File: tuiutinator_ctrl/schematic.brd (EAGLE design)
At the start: 87.3 x 63.5 mm, 13 parts

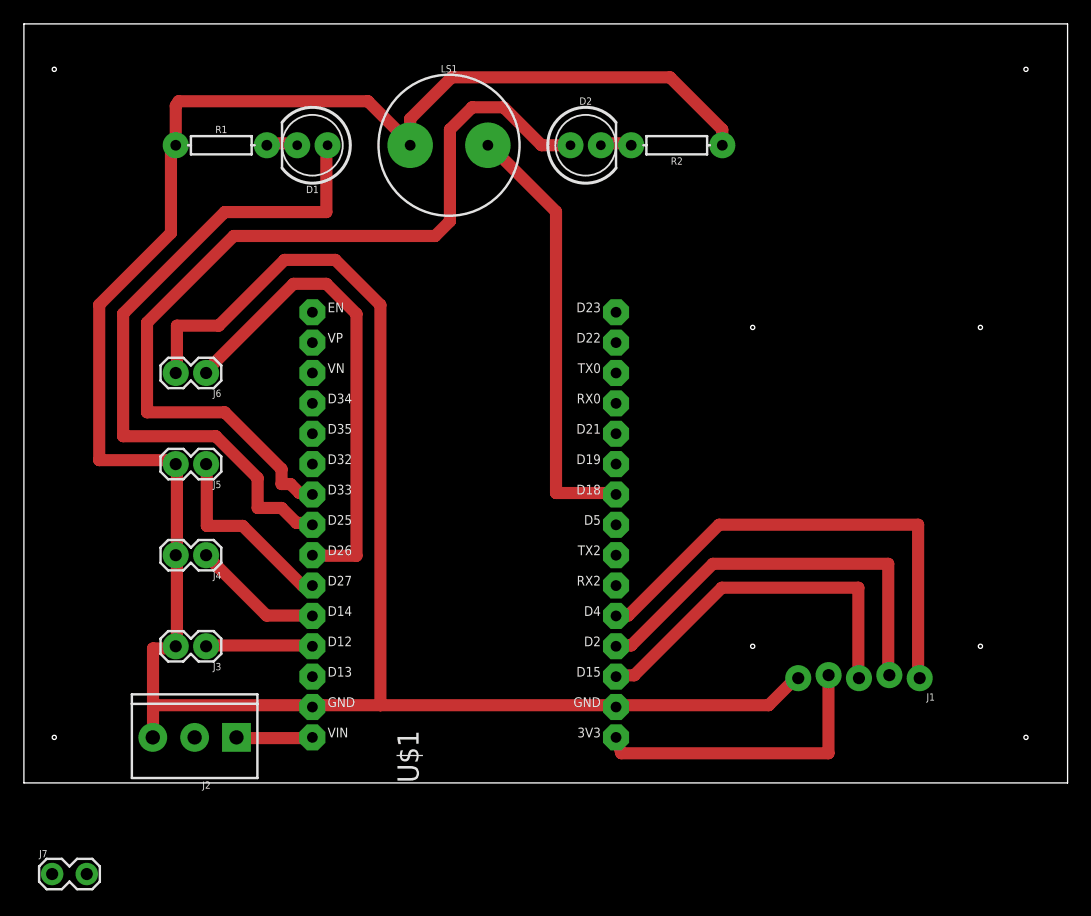
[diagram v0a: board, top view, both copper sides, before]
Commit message: Versão com controle pronto enviado para JLC
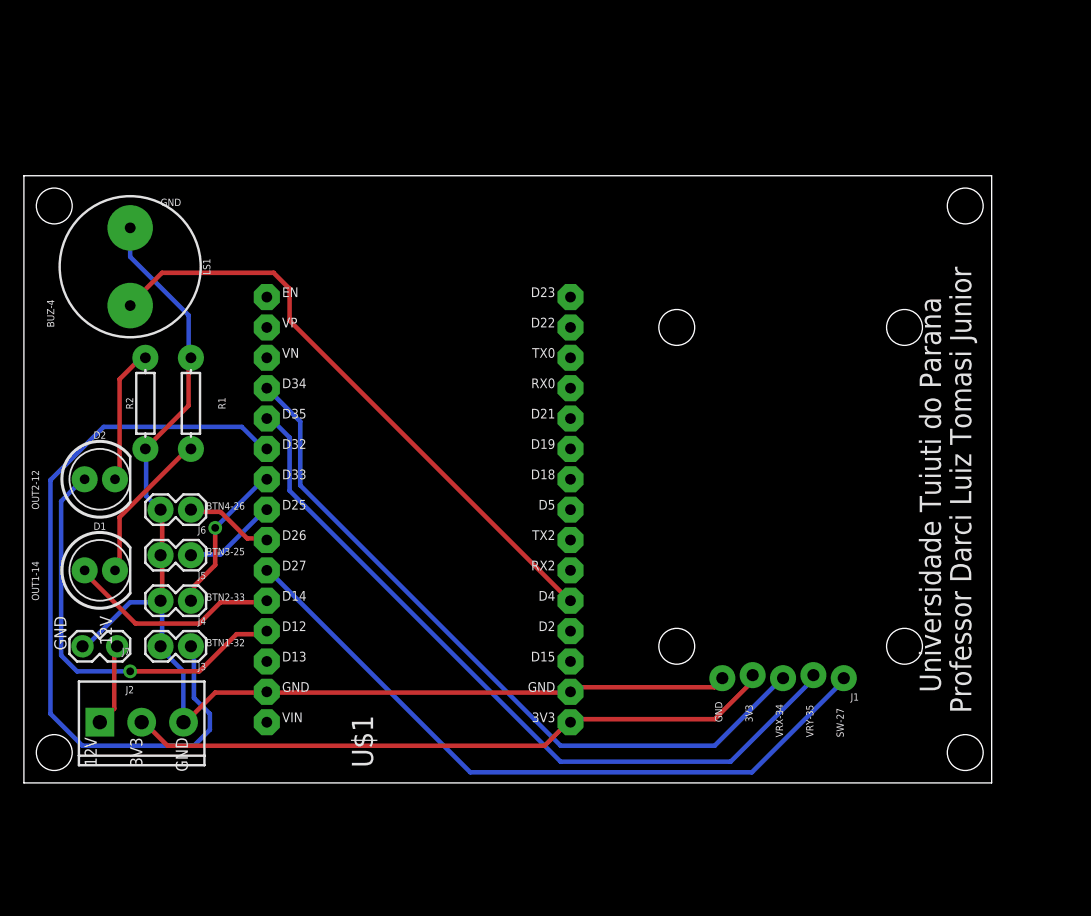
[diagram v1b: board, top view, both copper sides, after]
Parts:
- moved R2 49.4 mm to (10.2, 31.8), turned to 90 degrees
- moved D2 49.3 mm to (6.35, 25.4)
- moved D1 39.8 mm to (6.35, 17.8), turned to 0 degrees
- moved LS1 28.5 mm to (8.89, 43.2), turned to 270 degrees
- moved R1 21.7 mm to (14.0, 31.8), turned to 270 degrees
- moved J7 19.7 mm to (7.62, 11.4), turned to 180 degrees
- moved J2 11.5 mm to (6.35, 5.08), turned to 0 degrees
- moved J6 11.5 mm to (14.0, 22.9)
- moved J5 7.73 mm to (14.0, 19.1)
- moved J1 6.35 mm to (68.6, 8.89)
- moved U$1 4.02 mm to (34.3, 22.9)
- moved J4 4.02 mm to (14.0, 15.2)
- moved J3 1.27 mm to (14.0, 11.4)
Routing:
- net GND: track 231.4 -> 101.6 mm
- net BTN_1: track 8.84 -> 62.9 mm
- net OUT_2: track 73.7 -> 34.7 mm, vias 0 -> 1
- net OUT_1: track 56.6 -> 18.2 mm
- net BTN_4: track 40.5 -> 7.36 mm
- net VRX: track 30.9 -> 61.0 mm
- net 3V3: track 25.3 -> 55.1 mm
- net VRY: track 34.9 -> 63.6 mm
- net SW: track 41.3 -> 58.6 mm
- net BUZ: track 36.3 -> 50.9 mm
- net N$1: track 2.70 -> 13.2 mm
- net N$2: track 2.82 -> 11.4 mm
- net BTN_3: track 16.0 -> 7.88 mm
- net BTN_2: track 10.9 -> 12.9 mm, vias 0 -> 1
- net 12V: track 6.31 -> 6.95 mm
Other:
- board size 87.3 x 63.5 mm -> 81 x 50.8 mm
- board text added: "12V"
- board text added: "3V3"
- board text added: "BTN1-32"
- board text added: "BTN2-33"
- board text added: "BTN3-25"
- board text added: "BTN4-26"
- board text added: "BUZ-4"
- board text added: "GND"
- board text added: "OUT1-14"
- board text added: "OUT2-12"
- board text added: "Professor Darci Luiz Tomasi Junior"
- board text added: "SW-27"
- board text added: "Universidade Tuiuti do Parana"
- board text added: "VRX-34"
- board text added: "VRY-35"
